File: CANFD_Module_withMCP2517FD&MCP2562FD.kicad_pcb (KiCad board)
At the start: 2 copper layers, 27.9 x 25.4 mm, 14 parts, among them J1 Conn_01x05_Pin, J2 Conn_01x05_Pin, SW1 SW_DPDT_x2, U1 MCP2562-E-SN, U2 MCP2517FD-xSL, U4 LM1117MP-3.3

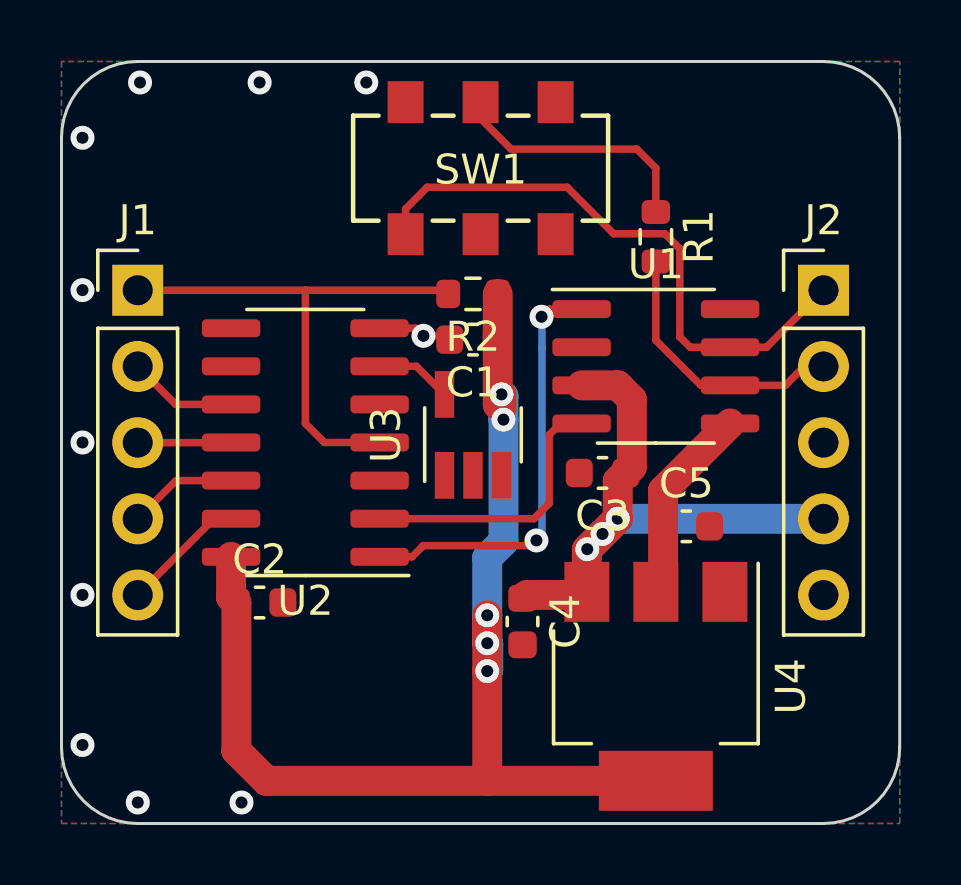
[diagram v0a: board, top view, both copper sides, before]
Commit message: add via
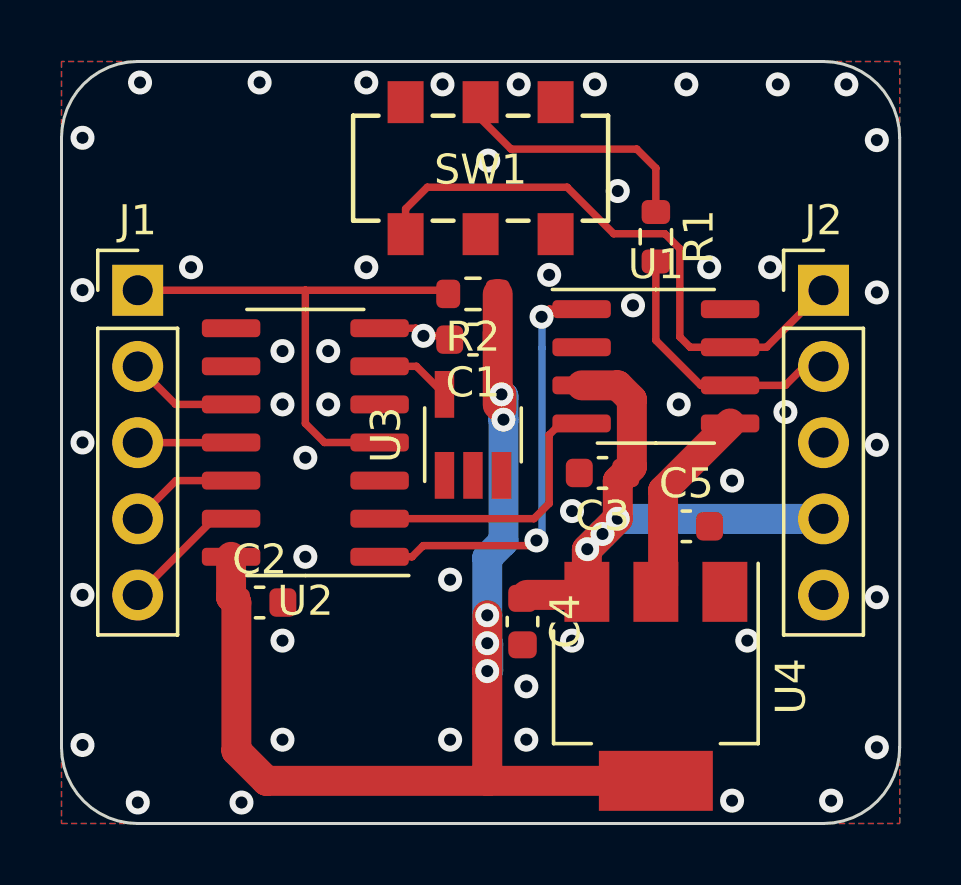
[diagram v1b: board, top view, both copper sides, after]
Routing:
- net GND: vias 11 -> 50
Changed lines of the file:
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@@
   (segment (start 124.903 72.39) (end 126.111 72.39) (width 0.25) (layer "F.Cu") (net 2))
   (segment (start 127.114 72.644) (end 127.241 72.771) (width 0.25) (layer "F.Cu") (net 2))
+  (via (at 132.842 67.818) (size 0.8) (drill 0.4) (layers "F.Cu" "B.Cu") (free) (net 2))
+  (via (at 136.652 77.47) (size 0.8) (drill 0.4) (layers "F.Cu" "B.Cu") (free) (net 2))
   (via (at 115 81.28) (size 0.8) (drill 0.4) (layers "F.Cu" "B.Cu") (free) (net 2))
+  (via (at 132.08 64.262) (size 0.8) (drill 0.4) (layers "F.Cu" "B.Cu") (free) (net 2))
+  (via (at 122.428 76.708) (size 0.8) (drill 0.4) (layers "F.Cu" "B.Cu") (free) (net 2))
+  (via (at 122.428 80.01) (size 0.8) (drill 0.4) (layers "F.Cu" "B.Cu") (free) (net 2))
+  (via (at 141.478 71.197379) (size 0.8) (drill 0.4) (layers "F.Cu" "B.Cu") (free) (net 2))
+  (via (at 124.46 70.358) (size 0.8) (drill 0.4) (layers "F.Cu" "B.Cu") (free) (net 2))
+  (via (at 131.318 78.486) (size 0.8) (drill 0.4) (layers "F.Cu" "B.Cu") (free) (net 2))
+  (via (at 135.89 70.358) (size 0.8) (drill 0.4) (layers "F.Cu" "B.Cu") (free) (net 2))
   (via (at 115 71.12) (size 0.8) (drill 0.4) (layers "F.Cu" "B.Cu") (free) (net 2))
+  (via (at 128.524 66.802) (size 0.8) (drill 0.4) (layers "F.Cu" "B.Cu") (free) (net 2))
+  (via (at 133.35 71.628) (size 0.8) (drill 0.4) (layers "F.Cu" "B.Cu") (free) (net 2))
+  (via (at 141.478037 66.120278) (size 0.8) (drill 0.4) (layers "F.Cu" "B.Cu") (free) (net 2))
+  (via (at 137.16 82.804) (size 0.8) (drill 0.4) (layers "F.Cu" "B.Cu") (free) (net 2))
+  (via (at 123.19 74.93) (size 0.8) (drill 0.4) (layers "F.Cu" "B.Cu") (free) (net 2))
+  (via (at 129.54 64.262) (size 0.8) (drill 0.4) (layers "F.Cu" "B.Cu") (free) (net 2))
+  (via (at 137.922 70.358) (size 0.8) (drill 0.4) (layers "F.Cu" "B.Cu") (free) (net 2))
+  (via (at 121.666 73.152) (size 0.8) (drill 0.4) (layers "F.Cu" "B.Cu") (free) (net 2))
+  (via (at 140.462 64.262) (size 0.8) (drill 0.4) (layers "F.Cu" "B.Cu") (free) (net 2))
+  (via (at 121.666 74.93) (size 0.8) (drill 0.4) (layers "F.Cu" "B.Cu") (free) (net 2))
+  (via (at 127.254 86.106) (size 0.8) (drill 0.4) (layers "F.Cu" "B.Cu") (free) (net 2))
+  (via (at 127 64.262) (size 0.8) (drill 0.4) (layers "F.Cu" "B.Cu") (free) (net 2))
+  (via (at 138.176 64.262) (size 0.8) (drill 0.4) (layers "F.Cu" "B.Cu") (free) (net 2))
   (via (at 115 76.2) (size 0.8) (drill 0.4) (layers "F.Cu" "B.Cu") (free) (net 2))
+  (via (at 139.954 88.138) (size 0.8) (drill 0.4) (layers "F.Cu" "B.Cu") (free) (net 2))
+  (via (at 129.794 84.328) (size 0.8) (drill 0.4) (layers "F.Cu" "B.Cu") (free) (net 2))
+  (via (at 141.478 86.36) (size 0.8) (drill 0.4) (layers "F.Cu" "B.Cu") (free) (net 2))
+  (via (at 136.652 88.138) (size 0.8) (drill 0.4) (layers "F.Cu" "B.Cu") (free) (net 2))
+  (via (at 131.318 82.804) (size 0.8) (drill 0.4) (layers "F.Cu" "B.Cu") (free) (net 2))
+  (via (at 129.794 86.106) (size 0.8) (drill 0.4) (layers "F.Cu" "B.Cu") (free) (net 2))
+  (via (at 141.478 81.357379) (size 0.8) (drill 0.4) (layers "F.Cu" "B.Cu") (free) (net 2))
   (via (at 120.904 64.2) (size 0.8) (drill 0.4) (layers "F.Cu" "B.Cu") (free) (net 2))
+  (via (at 135.128 64.262) (size 0.8) (drill 0.4) (layers "F.Cu" "B.Cu") (free) (net 2))
   (via (at 115 86.282621) (size 0.8) (drill 0.4) (layers "F.Cu" "B.Cu") (free) (net 2))
+  (via (at 121.666 82.804) (size 0.8) (drill 0.4) (layers "F.Cu" "B.Cu") (free) (net 2))
   (via (at 120.300119 88.200755) (size 0.8) (drill 0.4) (layers "F.Cu" "B.Cu") (free) (net 2))
+  (via (at 134.874 74.93) (size 0.8) (drill 0.4) (layers "F.Cu" "B.Cu") (free) (net 2))
   (via (at 115.000037 66.042899) (size 0.8) (drill 0.4) (layers "F.Cu" "B.Cu") (free) (net 2))
   (via (at 124.46 64.2) (size 0.8) (drill 0.4) (layers "F.Cu" "B.Cu") (free) (net 2))
+  (via (at 118.618 70.358) (size 0.8) (drill 0.4) (layers "F.Cu" "B.Cu") (free) (net 2))
+  (via (at 138.43 75.184) (size 0.8) (drill 0.4) (layers "F.Cu" "B.Cu") (free) (net 2))
+  (via (at 141.478 76.277379) (size 0.8) (drill 0.4) (layers "F.Cu" "B.Cu") (free) (net 2))
+  (via (at 123.19 73.152) (size 0.8) (drill 0.4) (layers "F.Cu" "B.Cu") (free) (net 2))
+  (via (at 127.254 80.772) (size 0.8) (drill 0.4) (layers "F.Cu" "B.Cu") (free) (net 2))
   (via (at 116.842899 88.199963) (size 0.8) (drill 0.4) (layers "F.Cu" "B.Cu") (free) (net 2))
   (via (at 126.365 72.644) (size 0.8) (drill 0.4) (layers "F.Cu" "B.Cu") (free) (net 2))
+  (via (at 121.666 86.106) (size 0.8) (drill 0.4) (layers "F.Cu" "B.Cu") (free) (net 2))
+  (via (at 130.556 70.612) (size 0.8) (drill 0.4) (layers "F.Cu" "B.Cu") (free) (net 2))
   (via (at 116.917379 64.2) (size 0.8) (drill 0.4) (layers "F.Cu" "B.Cu") (free) (net 2))
   (segment (start 129.807 81.28) (end 131.71 81.28) (width 1) (layer "F.Cu") (net 3))
